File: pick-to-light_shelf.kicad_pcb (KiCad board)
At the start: 4 copper layers, 39 parts, among them IC1 ATMEGA168PA-A, IC2 ENC28J60-C/SS, J1 RJ45-TRANSFO, P1 CONN_02X03, P2 CONN_02X03, U1 LD1117S33TR, Y1 Crystal, Y2 25MHz

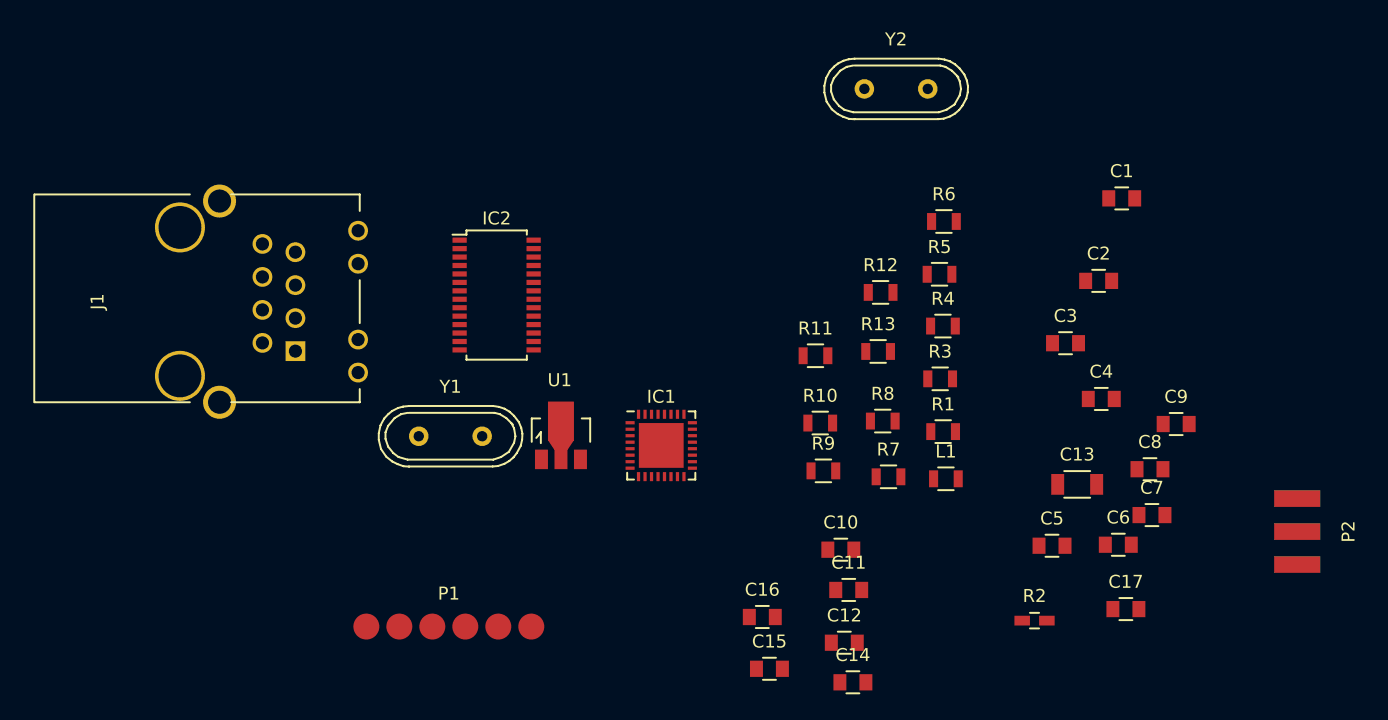
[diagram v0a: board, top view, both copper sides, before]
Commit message: Getting things up to date to start on project again
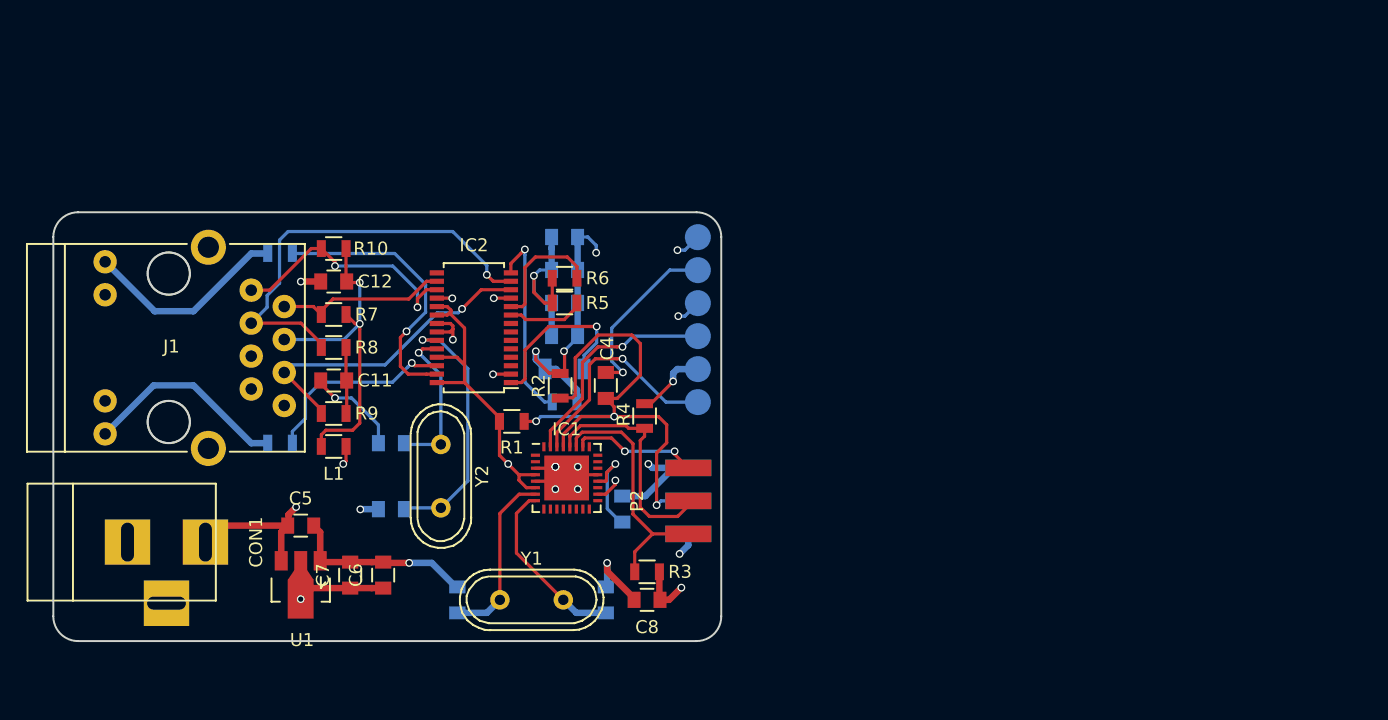
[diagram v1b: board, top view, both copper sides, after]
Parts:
- added CON1: 7.5V, Connect:BARREL_JACK, F.Cu at (90.5, 119.7)
- C1, C10, C13, C14, C15, C16, C17, C2, C3, C9, R11, R12, R13: moved to B.Cu
- IC1: footprint Housings_DFN_QFN:QFN-32-1EP_5x5mm_Pitch0.5mm -> PTL-footprints:QFN-32-1EP_5x5mm_Pitch0.5mm
- J1: footprint Connect:RJ45_TRANSFO -> PTL-footprints:HR911105A
- P1: value CONN_02X03 -> (none); moved to B.Cu
- P2: value CONN_02X03 -> (none)
- R2: footprint Capacitors_SMD:C_0603_HandSoldering -> Resistors_SMD:R_0805
- moved C7 61.9 mm to (107.8, 122.2), turned to 90 degrees
- moved C9 60.8 mm to (111.0, 117.1), turned to 180 degrees
- moved C1 59.8 mm to (116.1, 124.1), turned to 90 degrees
- moved C5 57.9 mm to (104.0, 118.4)
- moved C6 56.7 mm to (110.4, 122.2), turned to 90 degrees
- moved C17 51.9 mm to (124.4, 96.2)
- moved C12 48.2 mm to (106.6, 99.6)
- moved R12 47.7 mm to (102.4, 112.1), turned to 180 degrees
- moved L1 47.2 mm to (106.6, 112.3), turned to 180 degrees
- moved P2 46.9 mm to (133.9, 116.5), turned to 270 degrees
- moved Y2 46.0 mm to (114.8, 114.6), turned to 90 degrees
- moved C2 45.2 mm to (127.5, 124.1), turned to 90 degrees
- moved R7 44.5 mm to (106.6, 102.2)
- moved C11 42.8 mm to (106.6, 107.2), turned to 180 degrees
- moved R8 42.7 mm to (106.6, 104.7)
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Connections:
- J1 pad 2: Net-(C12-Pad2) -> /TPOUT-
- J1 pad 3: /TPOUT- -> /TPIN+
- J1 pad 4: /TPIN+ -> Net-(C12-Pad2)
- R11 pad 1: GND -> /LEDA
- R11 pad 2: Net-(J1-PadGK) -> Net-(J1-Pad9)
- R12 pad 1: GND -> /LEDB
- R12 pad 2: Net-(J1-PadYK) -> Net-(J1-Pad12)
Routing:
- net GND: track 0.00 -> 85.3 mm, vias 0 -> 20
- net VCC: track 0.00 -> 62.4 mm, vias 0 -> 7
- net /RAW: track 0.00 -> 44.6 mm, vias 0 -> 2
- net /RESET: track 0.00 -> 43.2 mm, vias 0 -> 3
- net /TPIN+: track 0.00 -> 33.7 mm, vias 0 -> 1
- net Net-(C12-Pad2): track 0.00 -> 26.3 mm, vias 0 -> 2
- net /TPIN-: track 0.00 -> 24.4 mm, vias 0 -> 1
- net /LEDA: track 0.00 -> 21.4 mm, vias 0 -> 1
- net Net-(C9-Pad1): track 0.00 -> 19.9 mm, vias 0 -> 1
- net /A4: track 0.00 -> 19.4 mm
- net /TPOUT+: track 0.00 -> 19.4 mm, vias 0 -> 2
- net /A5: track 0.00 -> 17.9 mm
- net /RX1: track 0.00 -> 17.2 mm, vias 0 -> 1
- net /TX0: track 0.00 -> 17.2 mm, vias 0 -> 1
- net Net-(J1-Pad9): track 0.00 -> 15.9 mm
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- added copper zone on Ground.plane, net GND
- added copper zone on Power.plane, net VCC
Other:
- board outline added: 51.4 x 33 mm
